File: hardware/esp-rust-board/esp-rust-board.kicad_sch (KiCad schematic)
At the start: 55 parts, among them J1 USB4105-GF-A, Q1 DMG3415U, SW1 SW_Push, SW2 SW_Push, U1 SHTC3, U2 ICM-42670-P, U3 ESP32-C3-MINI-1, U4 Rust_Board, U5 SY8088, U6 MCP73831T-2ACI/OT, Y1 32.768Hz

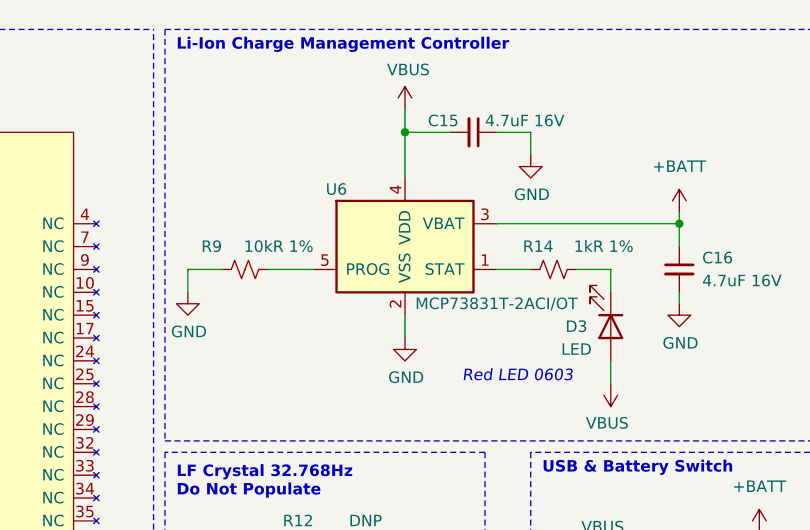
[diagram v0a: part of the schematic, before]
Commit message: Clean up, update symbols and footprints, port to Kicad 8.0
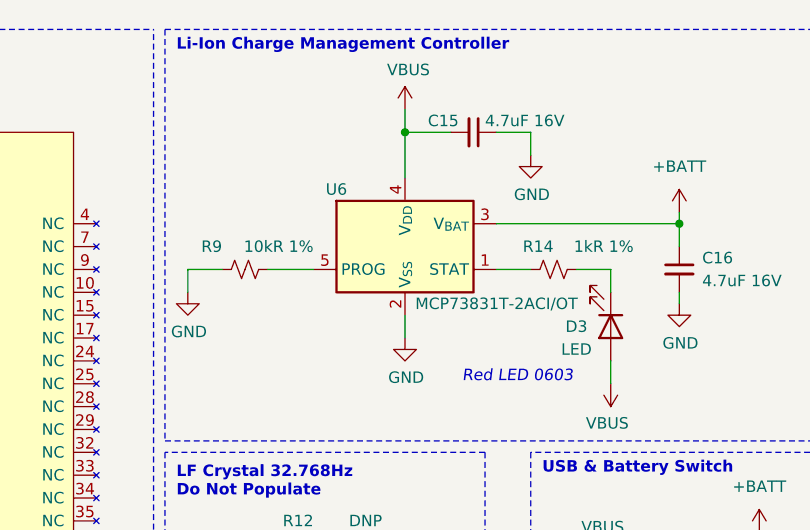
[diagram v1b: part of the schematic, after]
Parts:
- U1: footprint Rust_Board:SON100P200X200X80-5N -> Sensor_Humidity:Sensirion_DFN-4-1EP_2x2mm_P1mm_EP0.7x1.6mm
- U3: footprint Espressif:ESP32-C3-MINI-1 -> Rust_Board:ESP32-C3-MINI-1; symbol Espressif:ESP32-C3-MINI-1 -> Rust_Board:ESP32-C3-MINI-1

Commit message: Solve remaining  errors and warnings
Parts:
- U2: footprint Rust_Board:IC_ICM-42670-P -> IC_ICM-42670-P

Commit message: Update package
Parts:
- U2: footprint IC_ICM-42670-P -> Package_LGA:LGA-14_3x2.5mm_P0.5mm_LayoutBorder3x4y
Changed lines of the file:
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@@
 			)
 		)
-		(property "Footprint" "IC_ICM-42670-P"
+		(property "Footprint" "Package_LGA:LGA-14_3x2.5mm_P0.5mm_LayoutBorder3x4y"
 			(at 58.42 194.31 0)
 			(effects

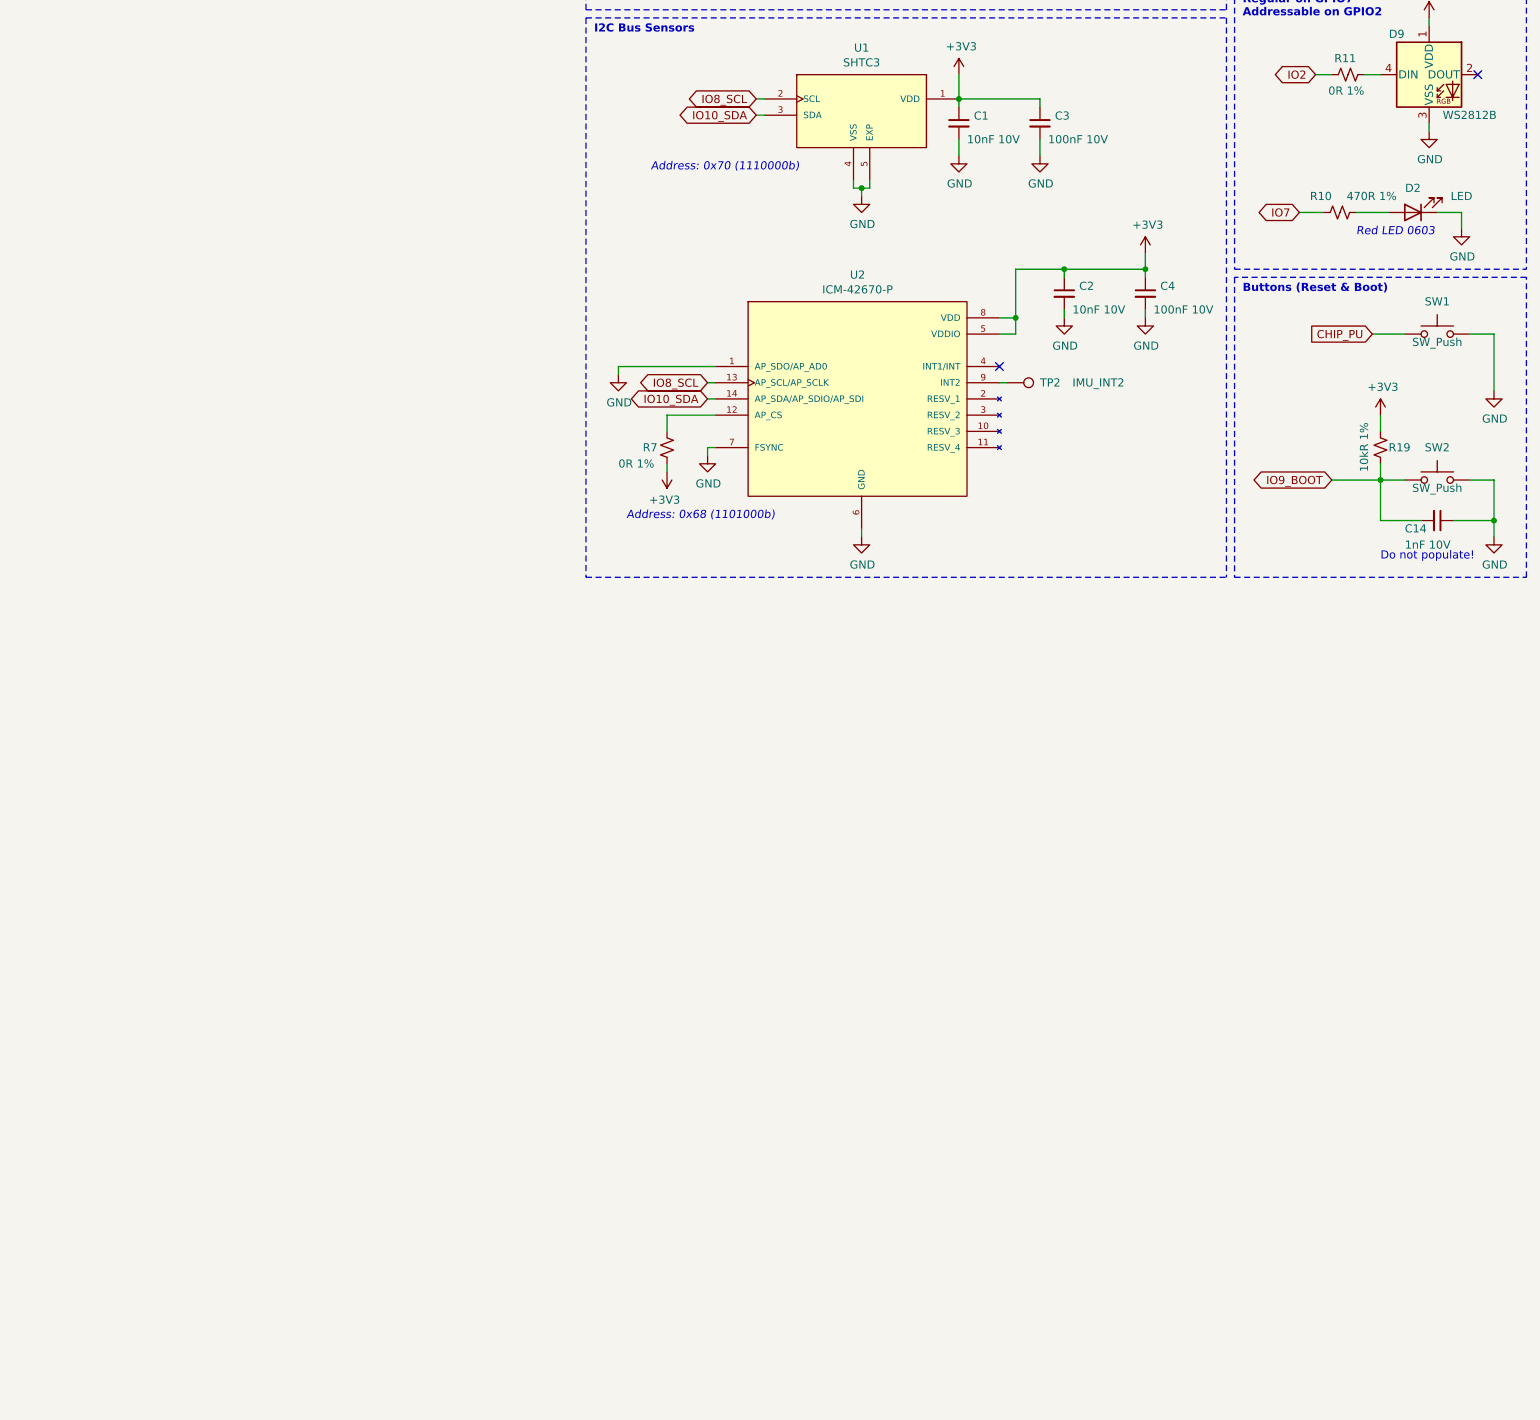
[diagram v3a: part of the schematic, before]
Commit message: Add new components
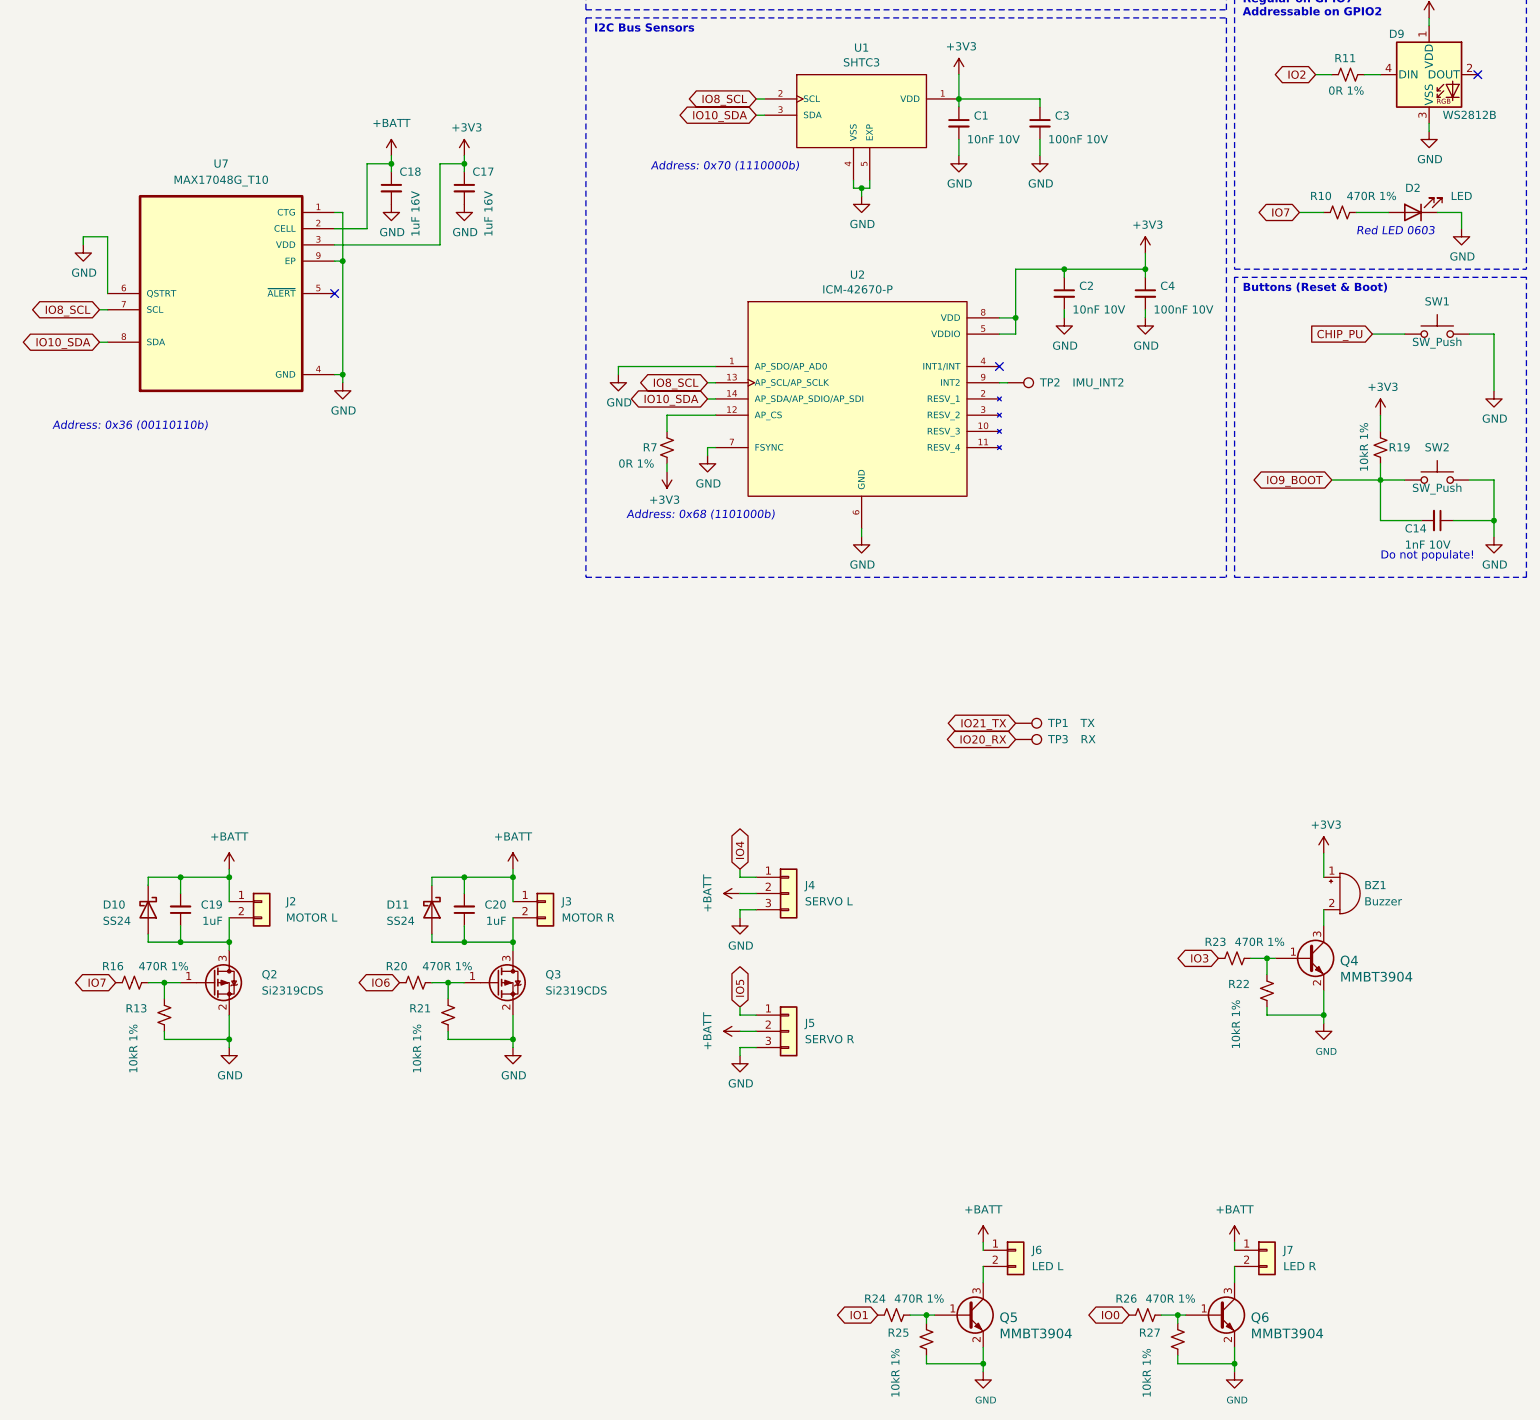
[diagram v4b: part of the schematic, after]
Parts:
- added BZ1: Buzzer, Rust_Board:MLT-5020, symbol Device:Buzzer
- added C17, C18: 1uF 16V, Capacitor_SMD:C_0402_1005Metric, symbol Device:C_Small
- added C19, C20: 1uF, Capacitor_SMD:C_0402_1005Metric, symbol Device:C_Small
- added D10, D11: SS24, Diode_SMD:D_SMA, symbol Diode:SS24
- added J2: MOTOR L, Connector_JST:JST_PH_B2B-PH-SM4-TB_1x02-1MP_P2.00mm_Vertical, symbol Connector_Generic:Conn_01x02
- added J3: MOTOR R, Connector_JST:JST_PH_B2B-PH-SM4-TB_1x02-1MP_P2.00mm_Vertical, symbol Connector_Generic:Conn_01x02
- added J4: SERVO L, Connector_JST:JST_PH_B3B-PH-SM4-TB_1x03-1MP_P2.00mm_Vertical, symbol Connector_Generic:Conn_01x03
- added J5: SERVO R, Connector_JST:JST_PH_B3B-PH-SM4-TB_1x03-1MP_P2.00mm_Vertical, symbol Connector_Generic:Conn_01x03
- added J6: LED L, Connector_JST:JST_PH_B2B-PH-SM4-TB_1x02-1MP_P2.00mm_Vertical, symbol Connector_Generic:Conn_01x02
- added J7: LED R, Connector_JST:JST_PH_B2B-PH-SM4-TB_1x02-1MP_P2.00mm_Vertical, symbol Connector_Generic:Conn_01x02
- added Q2, Q3: Si2319CDS, Package_TO_SOT_SMD:SOT-23, symbol Transistor_FET:Si2319CDS
- added Q4, Q5, Q6: MMBT3904, Package_TO_SOT_SMD:SOT-23, symbol Transistor_BJT:MMBT3904
- added R13, R21, R22, R25, R27: 10kR 1%, Resistor_SMD:R_0402_1005Metric, symbol Device:R_Small_US
- added R16, R20, R23, R24, R26: 470R 1%, Resistor_SMD:R_0402_1005Metric, symbol Device:R_Small_US
- added TP1: TX, TestPoint:TestPoint_Pad_D1.0mm, symbol Connector:TestPoint
- added TP3: RX, TestPoint:TestPoint_Pad_D1.0mm, symbol Connector:TestPoint
- added U7: MAX17048G_T10, Package_DFN_QFN:TDFN-8-1EP_2x2mm_P0.5mm_EP0.8x1.2mm, symbol Rust_Board:MAX17048G_T10
- D1: footprint Rust_Board:SOD-882 -> Diode_SMD:D_SOD-882
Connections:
- net +3V3: now also BZ1.1 (-), C17.1, U7.3 (VDD)
- net +BATT: now also C18.1, C19.2, C20.2, D10.1 (K), D11.1 (K), J2.1 (Pin_1), J3.1 (Pin_1), J4.2 (Pin_2), J5.2 (Pin_2), J6.1 (Pin_1), J7.1 (Pin_1), U7.2 (CELL)
- net GND: now also C17.2, C18.2, J4.3 (Pin_3), J5.3 (Pin_3), Q2.2 (S), Q3.2 (S), Q4.2 (E), Q5.2 (E), Q6.2 (E), R13.2, R21.2, R22.2, R25.2, R27.2, U7.1 (CTG), U7.4 (GND), U7.6 (QSTRT), U7.9 (EP)
- net IO0: now also R26.1
- net IO1: now also R24.1
- net IO10_SDA: now also U7.8 (SDA)
- net IO20_RX: now also TP3.1
- net IO21_TX: now also TP1.1
- net IO3: now also R23.1
- net IO4: now also J4.1 (Pin_1)
- net IO5: now also J5.1 (Pin_1)
- net IO6: now also R20.1
- net IO7: now also R16.1
- net IO8_SCL: now also U7.7 (SCL)
- new net: Q3.1 (G), R20.2, R21.1
- new net: C19.1, D10.2 (A), J2.2 (Pin_2), Q2.3 (D)
- new net: Q2.1 (G), R13.1, R16.2
- new net: J7.2 (Pin_2), Q6.3 (C)
- new net: Q5.1 (B), R24.2, R25.1
- new net: J6.2 (Pin_2), Q5.3 (C)
- new net: Q4.1 (B), R22.1, R23.2
- new net: C20.1, D11.2 (A), J3.2 (Pin_2), Q3.3 (D)
- new net: Q6.1 (B), R26.2, R27.1
- new net: BZ1.2 (+), Q4.3 (C)
- no-connect marks 9 -> 10
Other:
- note added: "Address: 0x36 (00110110b)"

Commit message: Work in progress
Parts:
- removed C12, C13: DNP, Capacitor_SMD:C_0402_1005Metric, symbol Device:C_Small
- removed C19, C20: 1uF, Capacitor_SMD:C_0402_1005Metric, symbol Device:C_Small
- removed D10, D11: SS24, Diode_SMD:D_SMA, symbol Diode:SS24
- removed D9: WS2812B, LED_SMD:LED_SK6812MINI_PLCC4_3.5x3.5mm_P1.75mm, symbol LED:WS2812B
- removed J2: MOTOR L, Connector_JST:JST_PH_B2B-PH-SM4-TB_1x02-1MP_P2.00mm_Vertical, symbol Connector_Generic:Conn_01x02
- removed J3: MOTOR R, Connector_JST:JST_PH_B2B-PH-SM4-TB_1x02-1MP_P2.00mm_Vertical, symbol Connector_Generic:Conn_01x02
- removed J4: SERVO L, Connector_JST:JST_PH_B3B-PH-SM4-TB_1x03-1MP_P2.00mm_Vertical, symbol Connector_Generic:Conn_01x03
- removed J5: SERVO R, Connector_JST:JST_PH_B3B-PH-SM4-TB_1x03-1MP_P2.00mm_Vertical, symbol Connector_Generic:Conn_01x03
- removed J6: LED L, Connector_JST:JST_PH_B2B-PH-SM4-TB_1x02-1MP_P2.00mm_Vertical, symbol Connector_Generic:Conn_01x02
- removed J7: LED R, Connector_JST:JST_PH_B2B-PH-SM4-TB_1x02-1MP_P2.00mm_Vertical, symbol Connector_Generic:Conn_01x02
- removed Q2, Q3: Si2319CDS, Package_TO_SOT_SMD:SOT-23, symbol Transistor_FET:Si2319CDS
- removed Q5, Q6: MMBT3904, Package_TO_SOT_SMD:SOT-23, symbol Transistor_BJT:MMBT3904
- removed R12: DNP, Resistor_SMD:R_0402_1005Metric, symbol Device:R_Small_US
- removed R13, R21, R25, R27: 10kR 1%, Resistor_SMD:R_0402_1005Metric, symbol Device:R_Small_US
- removed R16, R20, R24, R26: 470R 1%, Resistor_SMD:R_0402_1005Metric, symbol Device:R_Small_US
- removed TP1: TX, TestPoint:TestPoint_Pad_D1.0mm, symbol Connector:TestPoint
- removed TP3: RX, TestPoint:TestPoint_Pad_D1.0mm, symbol Connector:TestPoint
- removed Y1: 32.768Hz, Crystal:Crystal_SMD_3215-2Pin_3.2x1.5mm, symbol Device:Crystal
- added D9: LED, LED_SMD:LED_0603_1608Metric, symbol Device:LED
- added J2, J3: DF37C-30DP-0.4V_51_, Rust_Board:HRS_DF37C-30DP-0.4V_51_, symbol DF37C-30DP-0.4V_51_:DF37C-30DP-0.4V_51_
- added J8: BATTERY, Connector_JST:JST_EH_B2B-EH-A_1x02_P2.50mm_Vertical, symbol Connector_Generic:Conn_01x02
- R11: value 0R 1% -> 470R 1%; LCSC C17168 -> C25117
- SW1: value SW_Push -> RESET
- SW2: value SW_Push -> BOOT
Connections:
- net +3V3: now also R10.1
- net +5V: now also J3.1, J3.11, J3.13, J3.15, J3.17, J3.19, J3.21, J3.23, J3.25, J3.27, J3.29, J3.3, J3.5, J3.7, J3.9
- net +BATT: now also J3.10, J3.12, J3.14, J3.16, J3.18, J3.2, J3.20, J3.22, J3.24, J3.26, J3.28, J3.30, J3.4, J3.6, J3.8, J8.1 (Pin_1); no longer U4.28 (VBAT)
- net GND: now also D9.1 (K), J2.1, J2.11, J2.13, J2.15, J2.17, J2.19, J2.21, J2.23, J2.25, J2.27, J2.29, J2.3, J2.5, J2.7, J2.9, J8.2 (Pin_2)
- net IO10_SDA: no longer U4.17 (SDA/GPIO10)
- net IO7: no longer R10.1
- net IO8_SCL: no longer U4.18 (SCL/GPIO8)
- net USB_D+: no longer U4.19 (USB_D+/GPIO19)
- net USB_D-: no longer U4.20 (USB_D-/GPIO18)
- net VBUS: no longer U4.26 (VBUS)
- net at R11.2: now also D9.2 (A)
- net ENABLE: no longer names the net of R1.2, U5.1 (EN)
- net ENABLE: no longer U4.27 (ENABLE)
- no-connect marks 10 -> 16
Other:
- note added: "Buzzer"
- note removed: "LF Crystal 32.768Hz Do Not Populate"
- company: Espressif -> (none)
- title: ESP32-C3-DevKit-RUST-1 -> (none)
- moved on the sheet: BZ1, C5, C6, C7, L1, Q4, R1, R11, R2, R22, R23, R3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

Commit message: Add magnamometer and barometer and rearrange items
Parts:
- added C12: 10nF 10V, Capacitor_SMD:C_0402_1005Metric, symbol Device:C_Small
- added C13: 100nF 10V, Capacitor_SMD:C_0402_1005Metric, symbol Device:C_Small
- added C19: 4.7uF 16V, Capacitor_SMD:C_0603_1608Metric, symbol Device:C_Small
- added C20: 10uF 16V, Capacitor_SMD:C_0805_2012Metric, symbol Device:C_Small
- added C21: 0.22uF, Capacitor_SMD:C_0402_1005Metric, symbol Device:C_Small
- added R12: 10kR 1%, Resistor_SMD:R_0402_1005Metric, symbol Device:R_Small_US
- added SW3: SW_DPDT_x2, Rust_Board:SW_SPDT_PCM12, symbol Switch:SW_DPDT_x2
- added U8: BMP280, Package_LGA:Bosch_LGA-8_2x2.5mm_P0.65mm_ClockwisePinNumbering, symbol Sensor_Pressure:BMP280
- added U9: QMC5883L, Package_LGA:LGA-16_3x3mm_P0.5mm, symbol Rust_Board:QMC5883L
- J2: value DF37C-30DP-0.4V_51_ -> GPIO; LCSC (none) -> C324722
- J3: value DF37C-30DP-0.4V_51_ -> POWER; LCSC (none) -> C324722
- J8: footprint Connector_JST:JST_EH_B2B-EH-A_1x02_P2.50mm_Vertical -> Connector_JST:JST_XH_B2B-XH-AM_1x02_P2.50mm_Vertical
- U2: LCSC (none) -> C3288646
- U7: LCSC (none) -> C2682616
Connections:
- net +3V3: now also J2.1, J2.2, J2.3, J2.4, C12.1, C13.1, C20.1, R12.1, SW3.1 (A), U8.6 (VDDIO), U8.8 (VDD), U9.13 (VDDIO), U9.2 (VDD), U9.4 (S1); no longer BZ1.1 (-), C6.1, C7.1, L1.2, R2.1
- net +5V: now also BZ1.1 (-)
- net GND: now also C12.2, C13.2, C19.2, C20.2, U8.1 (GND), U8.5 (SDO), U8.7 (GND), U9.11 (GND), U9.9 (GND); no longer J2.1, J2.3, J2.5, J2.7, J2.9
- net IO0: now also J2.30; no longer U4.5 (A0/GPIO0)
- net IO1: now also J2.28; no longer U4.6 (A1/GPIO1)
- net IO10_SDA: now also J2.6, U8.3 (SDI), U9.16 (SDA)
- net IO2: now also J2.26; no longer U4.7 (A2/GPIO2)
- net IO20_RX: now also J2.10; no longer U4.15 (RXD/GPIO20)
- net IO21_TX: now also J2.12; no longer U4.14 (TXD/GPIO21)
- net IO3: now also J2.24; no longer U4.8 (A3/GPIO3)
- net IO4: now also J2.22; no longer U4.9 (A4/GPIO4)
- net IO5: now also J2.20; no longer U4.10 (A5/GPIO5)
- net IO6: now also J2.18; no longer U4.11 (GPIO6)
- net IO7: now also J2.16; no longer U4.12 (GPIO7)
- net IO8_SCL: now also J2.14, U8.4 (SCK), U9.1 (SCL); no longer U4.13 (GPIO8)
- net IO9_BOOT: now also J2.8
- new net: R12.2, U8.2 (CSB)
- new net: C19.1, U9.10 (CAP)
- new net: C21.1, U9.12 (SETC)
- new net: C21.2, U9.8 (SETP)
- new net POWER: C6.1, C7.1, L1.2, R2.1, SW3.2 (B)
- no-connect marks 16 -> 21
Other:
- note added: "Address: 0x76 (1001100b)"
- moved on the sheet: C15, C16, C17, D3, J2, J8, R14, R9, U6
